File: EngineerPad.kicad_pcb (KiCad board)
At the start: 2 copper layers, 115 x 98 mm, 69 parts, among them J1 AVR ISP, J2 USB_A, SW1 SW_Push, SW10 SW_Push, SW11 SW_Push, SW12 SW_Push, SW13 SW_Push, SW14 SW_Push, SW15 SW_Push, SW16 SW_Push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

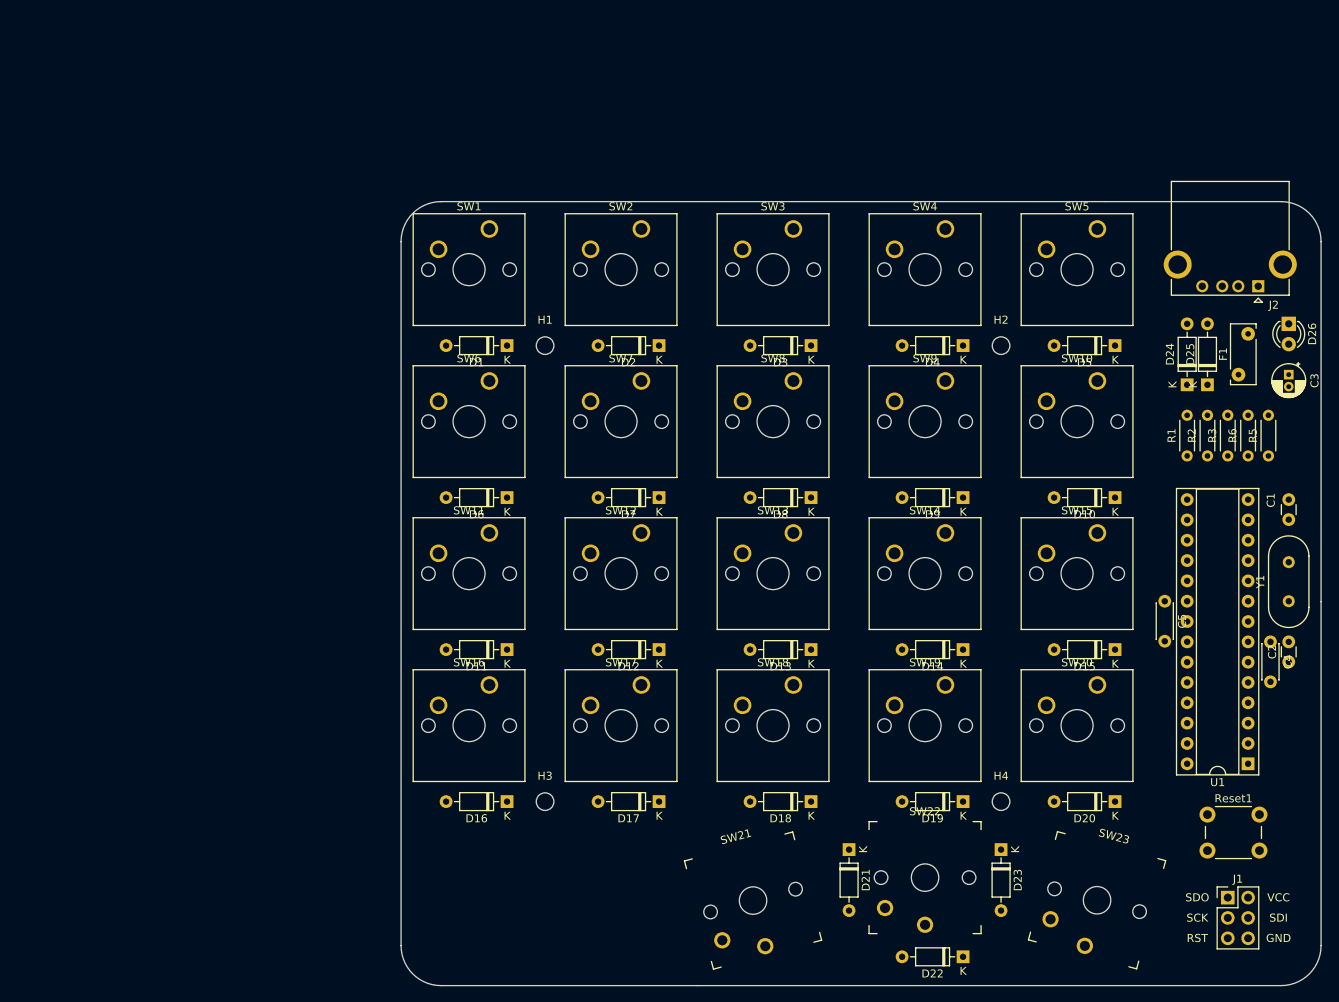
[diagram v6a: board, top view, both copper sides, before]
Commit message: inch based design
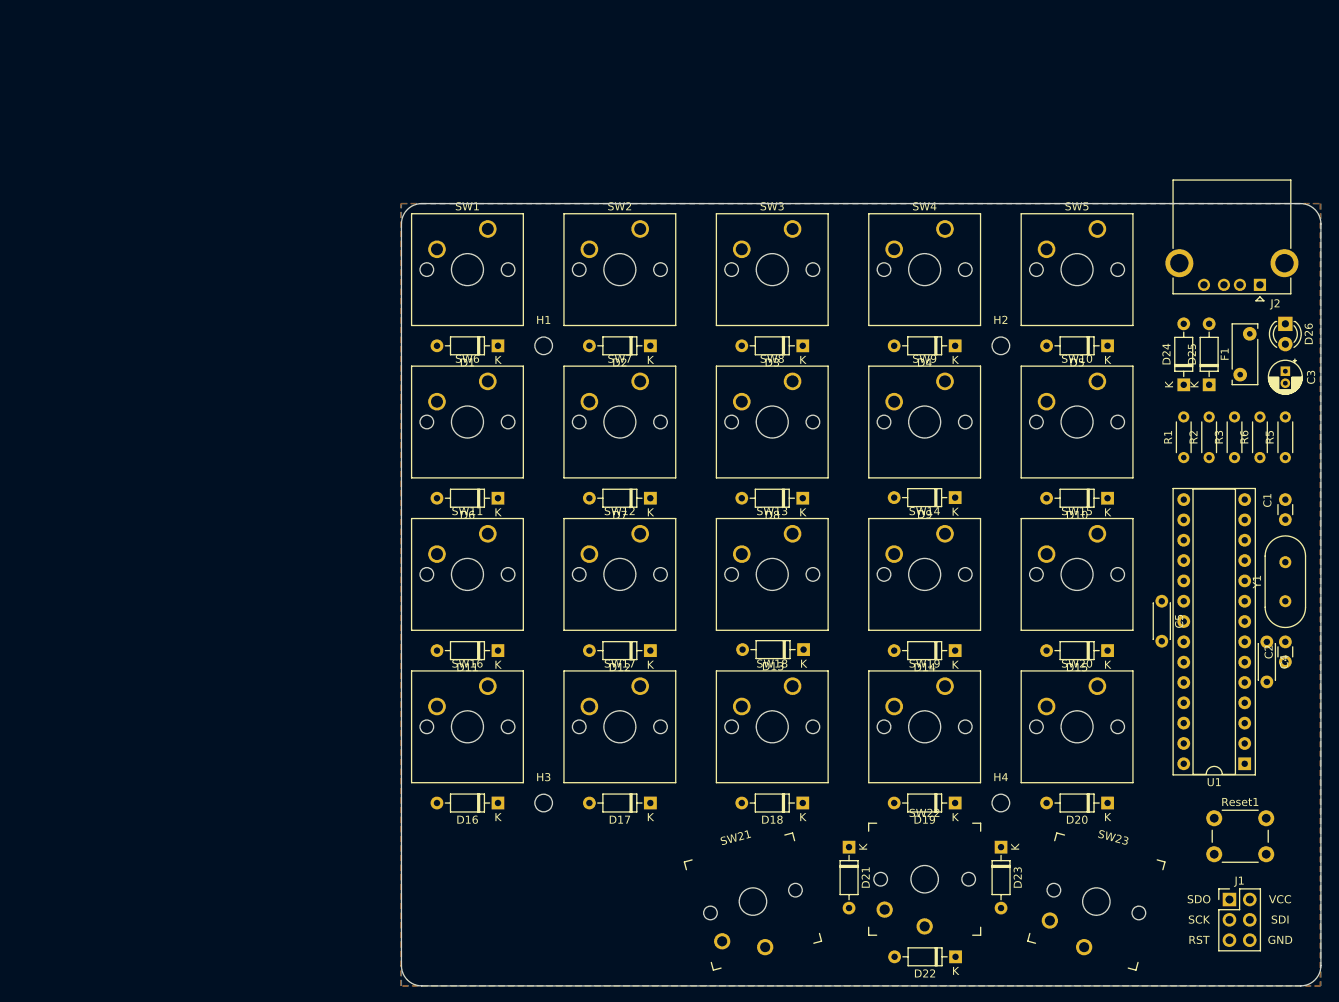
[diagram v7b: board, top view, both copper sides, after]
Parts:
- moved R5 2.13 mm to (187.5, 90.0)
- moved R6 1.49 mm to (184.4, 90.0)
- moved D16 1.15 mm to (89.1, 133.2)
- moved D11 1.15 mm to (89.1, 114.1)
- moved D6 1.14 mm to (89.1, 95.1)
- moved D1 1.14 mm to (89.1, 76.0)
- moved D17 1.10 mm to (108.2, 133.2)
- moved D12 1.10 mm to (108.2, 114.1)
- moved D7 1.09 mm to (108.2, 95.1)
- moved D2 1.09 mm to (108.2, 76.0)
- moved D18 1.05 mm to (127.2, 133.2)
- moved D8 1.04 mm to (127.2, 95.1)
- moved D3 1.04 mm to (127.2, 76.0)
- moved D19 1.01 mm to (146.3, 133.2)
- moved D14 1.00 mm to (146.3, 114.1)
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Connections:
- U1 pad 11: (no net) -> Net-(U1-Pad11)
- U1 pad 12: (no net) -> Net-(U1-Pad12)
- U1 pad 13: (no net) -> Net-(U1-Pad13)
- U1 pad 14: (no net) -> Net-(U1-Pad14)
- U1 pad 15: Row4 -> Row0
- U1 pad 16: Row3 -> Row1
- U1 pad 18: Row1 -> Row3
- U1 pad 19: Row0 -> Row4
- U1 pad 2: (no net) -> Net-(U1-Pad2)
- U1 pad 21: (no net) -> Net-(U1-Pad21)
- U1 pad 28: (no net) -> Net-(U1-Pad28)
- U1 pad 3: (no net) -> Net-(U1-Pad3)
- U1 pad 4: D- -> D+
- U1 pad 5: D+ -> D-
- U1 pad 6: (no net) -> Net-(U1-Pad6)
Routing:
- added copper zone on B.Cu, net GND
- added copper zone on F.Cu, net GND
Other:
- board size 115 x 98 mm -> 114.9 x 97.8 mm
- board text removed: "Keyswitch: 19mm Electronic Component: 100mil(0.254mm)"
